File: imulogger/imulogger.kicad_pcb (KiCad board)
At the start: 2 copper layers, 64 x 25 mm, 31 parts, among them J1 DEBUG, J2 BATCONN, J4 Micro_SD_Card, J5 PWRCONN, Q1 TP0610T, U1 ESP32-WROOM-32, U2 USFS, U3 MCP1826S, U4 MCP73831-2-OT

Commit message: pcb: remove excessive vias close to the IMU
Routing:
- net GND: vias 67 -> 27
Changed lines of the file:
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@@
     (thickness 1.6)
     (drawings 12)
-    (tracks 488)
+    (tracks 448)
     (zones 0)
     (modules 31)
@@
   (segment (start 151.274999 67.774999) (end 145.651999 67.774999) (width 0.25) (layer B.Cu) (net 1))
   (segment (start 154 70.5) (end 151.274999 67.774999) (width 0.25) (layer B.Cu) (net 1) (status 10))
+  (segment (start 165.80237 71.54) (end 166.88 71.54) (width 0.4) (layer B.Cu) (net 1))
+  (segment (start 165.225001 75.675001) (end 165.225001 72.117369) (width 0.4) (layer B.Cu) (net 1))
+  (segment (start 148.325 81.3) (end 148.325 82.3) (width 0.4) (layer B.Cu) (net 1))
+  (segment (start 165.225001 72.117369) (end 165.80237 71.54) (width 0.4) (layer B.Cu) (net 1))
+  (segment (start 166.4 82.3) (end 166.4 76.85) (width 0.4) (layer B.Cu) (net 1))
+  (segment (start 166.4 76.85) (end 165.225001 75.675001) (width 0.4) (layer B.Cu) (net 1))
+  (segment (start 148.325 82.3) (end 148.925 82.9) (width 0.4) (layer B.Cu) (net 1))
+  (segment (start 148.925 82.9) (end 165.8 82.9) (width 0.4) (layer B.Cu) (net 1))
+  (segment (start 165.8 82.9) (end 166.4 82.3) (width 0.4) (layer B.Cu) (net 1))
   (via (at 156.65 70.175) (size 0.8) (drill 0.4) (layers F.Cu B.Cu) (net 2))
   (via (at 156.65 79.975) (size 0.8) (drill 0.4) (layers F.Cu B.Cu) (net 2))
@@
   (via (at 164.5 71.5) (size 0.8) (drill 0.4) (layers F.Cu B.Cu) (net 2))
   (via (at 164.5 76.5) (size 0.8) (drill 0.4) (layers F.Cu B.Cu) (net 2))
-  (via (at 170.5 76.5) (size 0.8) (drill 0.4) (layers F.Cu B.Cu) (net 2))
-  (segment (start 165.80237 71.54) (end 166.88 71.54) (width 0.4) (layer B.Cu) (net 1))
-  (segment (start 165.225001 75.675001) (end 165.225001 72.117369) (width 0.4) (layer B.Cu) (net 1))
-  (segment (start 148.325 81.3) (end 148.325 82.3) (width 0.4) (layer B.Cu) (net 1))
-  (segment (start 165.225001 72.117369) (end 165.80237 71.54) (width 0.4) (layer B.Cu) (net 1))
-  (segment (start 166.4 82.3) (end 166.4 76.85) (width 0.4) (layer B.Cu) (net 1))
-  (segment (start 166.4 76.85) (end 165.225001 75.675001) (width 0.4) (layer B.Cu) (net 1))
-  (segment (start 148.325 82.3) (end 148.925 82.9) (width 0.4) (layer B.Cu) (net 1))
-  (segment (start 148.925 82.9) (end 165.8 82.9) (width 0.4) (layer B.Cu) (net 1))
-  (segment (start 165.8 82.9) (end 166.4 82.3) (width 0.4) (layer B.Cu) (net 1))
-  (via (at 178.5 76.5) (size 0.8) (drill 0.4) (layers F.Cu B.Cu) (net 2))
-  (via (at 168.5 80.5) (size 0.8) (drill 0.4) (layers F.Cu B.Cu) (net 2))
-  (via (at 170.5 78.5) (size 0.8) (drill 0.4) (layers F.Cu B.Cu) (net 2))
-  (via (at 170.5 80.5) (size 0.8) (drill 0.4) (layers F.Cu B.Cu) (net 2))
-  (via (at 172.5 78.5) (size 0.8) (drill 0.4) (layers F.Cu B.Cu) (net 2))
-  (via (at 172.5 80.5) (size 0.8) (drill 0.4) (layers F.Cu B.Cu) (net 2))
-  (via (at 174.5 78.5) (size 0.8) (drill 0.4) (layers F.Cu B.Cu) (net 2))
-  (via (at 174.5 80.5) (size 0.8) (drill 0.4) (layers F.Cu B.Cu) (net 2))
-  (via (at 176.5 78.5) (size 0.8) (drill 0.4) (layers F.Cu B.Cu) (net 2))
-  (via (at 176.5 80.5) (size 0.8) (drill 0.4) (layers F.Cu B.Cu) (net 2))
-  (via (at 178.5 78.5) (size 0.8) (drill 0.4) (layers F.Cu B.Cu) (net 2))
   (via (at 128.5 62.5) (size 0.8) (drill 0.4) (layers F.Cu B.Cu) (net 2))
   (via (at 141.75 72.55) (size 0.8) (drill 0.4) (layers F.Cu B.Cu) (net 2))
@@
   (segment (start 168.4 74.588) (end 167.892 74.08) (width 0.25) (layer B.Cu) (net 2))
   (segment (start 168.4 77.35) (end 168.4 74.588) (width 0.25) (layer B.Cu) (net 2))
-  (via (at 178.5 80.5) (size 0.8) (drill 0.4) (layers F.Cu B.Cu) (net 2))
-  (via (at 181 76.5) (size 0.8) (drill 0.4) (layers F.Cu B.Cu) (net 2))
-  (via (at 181 78.5) (size 0.8) (drill 0.4) (layers F.Cu B.Cu) (net 2))
-  (via (at 181 80.5) (size 0.8) (drill 0.4) (layers F.Cu B.Cu) (net 2))
-  (via (at 181 82.5) (size 0.8) (drill 0.4) (layers F.Cu B.Cu) (net 2))
-  (via (at 178.5 82.5) (size 0.8) (drill 0.4) (layers F.Cu B.Cu) (net 2))
-  (via (at 176.5 82.5) (size 0.8) (drill 0.4) (layers F.Cu B.Cu) (net 2))
-  (via (at 174.5 82.5) (size 0.8) (drill 0.4) (layers F.Cu B.Cu) (net 2))
-  (via (at 172.5 82.5) (size 0.8) (drill 0.4) (layers F.Cu B.Cu) (net 2))
-  (via (at 170.5 82.5) (size 0.8) (drill 0.4) (layers F.Cu B.Cu) (net 2))
-  (via (at 168.5 82.5) (size 0.8) (drill 0.4) (layers F.Cu B.Cu) (net 2))
-  (via (at 182 60.5) (size 0.8) (drill 0.4) (layers F.Cu B.Cu) (net 2))
-  (via (at 182 62) (size 0.8) (drill 0.4) (layers F.Cu B.Cu) (net 2))
-  (via (at 180 62) (size 0.8) (drill 0.4) (layers F.Cu B.Cu) (net 2))
-  (via (at 178 62) (size 0.8) (drill 0.4) (layers F.Cu B.Cu) (net 2))
-  (via (at 176 62) (size 0.8) (drill 0.4) (layers F.Cu B.Cu) (net 2))
-  (via (at 174 62) (size 0.8) (drill 0.4) (layers F.Cu B.Cu) (net 2))
-  (via (at 172 62) (size 0.8) (drill 0.4) (layers F.Cu B.Cu) (net 2))
-  (via (at 170 62) (size 0.8) (drill 0.4) (layers F.Cu B.Cu) (net 2))
-  (via (at 180 60.5) (size 0.8) (drill 0.4) (layers F.Cu B.Cu) (net 2))
-  (via (at 178 60.5) (size 0.8) (drill 0.4) (layers F.Cu B.Cu) (net 2))
-  (via (at 176 60.5) (size 0.8) (drill 0.4) (layers F.Cu B.Cu) (net 2))
-  (via (at 174 60.5) (size 0.8) (drill 0.4) (layers F.Cu B.Cu) (net 2))
-  (via (at 172 60.5) (size 0.8) (drill 0.4) (layers F.Cu B.Cu) (net 2))
-  (via (at 170 60.5) (size 0.8) (drill 0.4) (layers F.Cu B.Cu) (net 2))
-  (via (at 176.5 76.5) (size 0.8) (drill 0.4) (layers F.Cu B.Cu) (net 2))
-  (via (at 174.5 76.5) (size 0.8) (drill 0.4) (layers F.Cu B.Cu) (net 2))
-  (via (at 172.5 76.5) (size 0.8) (drill 0.4) (layers F.Cu B.Cu) (net 2))
   (segment (start 133.499999 62.075001) (end 132.174999 62.075001) (width 0.25) (layer F.Cu) (net 2))
   (segment (start 134.675 60.9) (end 133.499999 62.075001) (width 0.25) (layer F.Cu) (net 2))

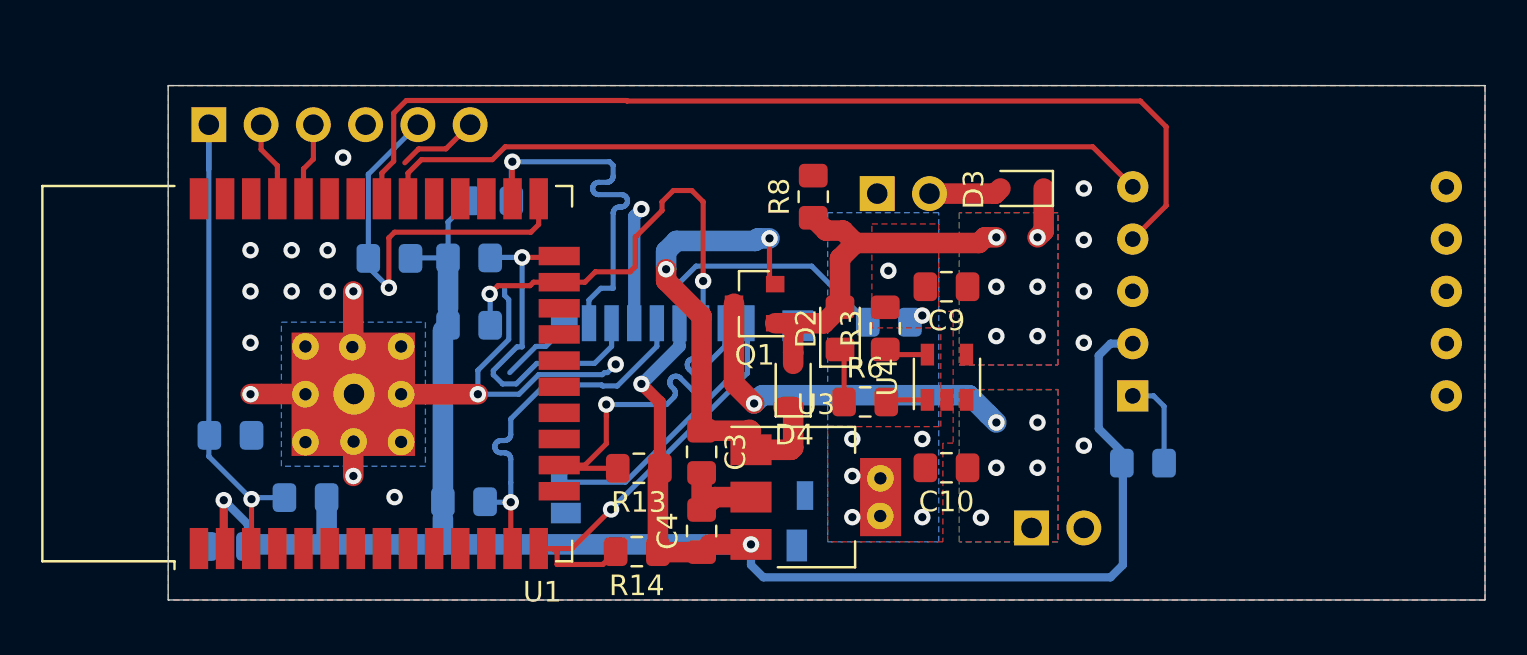
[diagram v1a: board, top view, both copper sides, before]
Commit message: imulogger: pcb: reroute i2c and optimize ground fillings
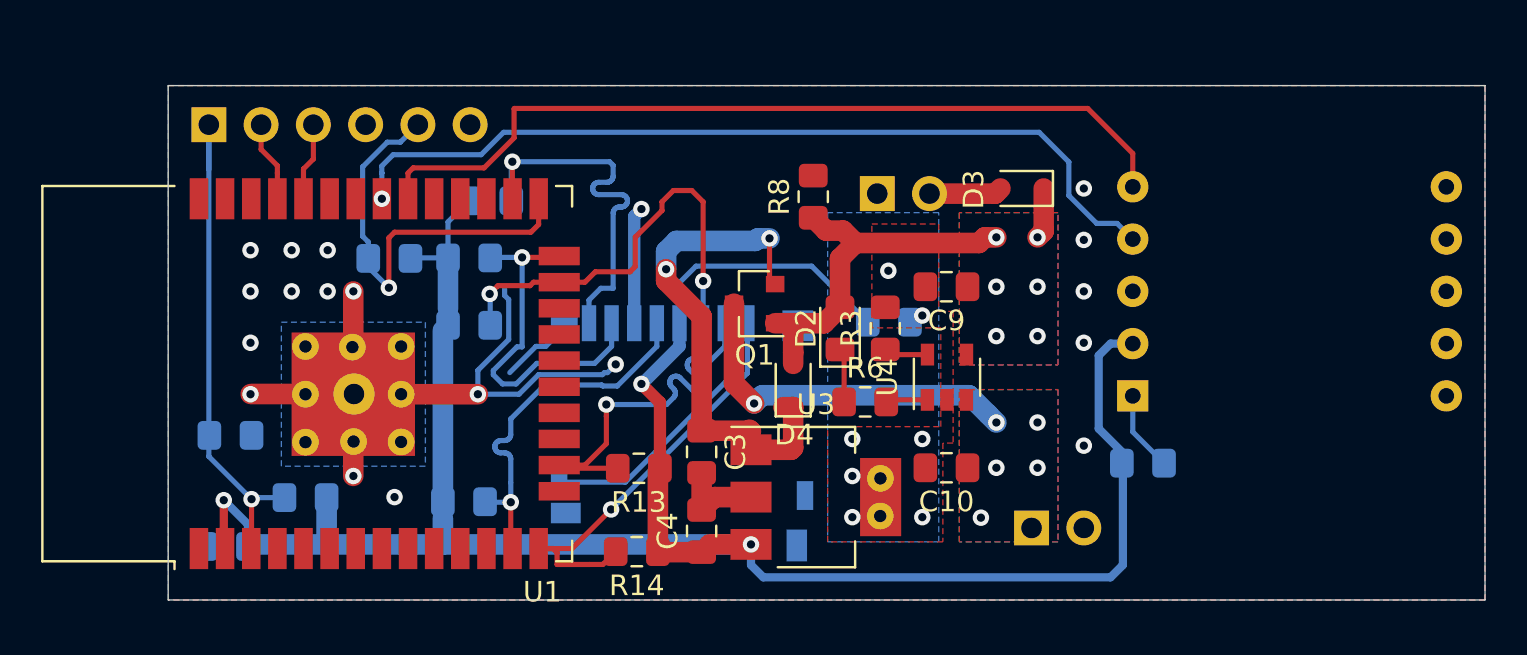
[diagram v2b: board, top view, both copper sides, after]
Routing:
- net IMU_SCL: track 48.9 -> 41.9 mm, vias 0 -> 1
- net GND: track 70.1 -> 65.6 mm, vias 27 -> 26
- net IMU_SDA: track 37.8 -> 41.1 mm
- net IO0: track 20.7 -> 21.3 mm
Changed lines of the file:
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@@
-(kicad_pcb (version 20171130) (host pcbnew 5.1.0)
+(kicad_pcb (version 20171130) (host pcbnew 5.1.2)
   (general
     (thickness 1.6)
     (drawings 12)
-    (tracks 448)
+    (tracks 453)
     (zones 0)
     (modules 31)
@@
     (last_trace_width 0.25)
     (trace_clearance 0.2)
-    (zone_clearance 0.5)
+    (zone_clearance 0.25)
     (zone_45_only no)
     (trace_min 0.2)
@@
   (via (at 164.5 71.5) (size 0.8) (drill 0.4) (layers F.Cu B.Cu) (net 2))
   (via (at 164.5 76.5) (size 0.8) (drill 0.4) (layers F.Cu B.Cu) (net 2))
-  (via (at 128.5 62.5) (size 0.8) (drill 0.4) (layers F.Cu B.Cu) (net 2))
   (via (at 141.75 72.55) (size 0.8) (drill 0.4) (layers F.Cu B.Cu) (net 2))
   (via (at 135.05 74) (size 0.8) (drill 0.4) (layers F.Cu B.Cu) (net 2))
@@
   (segment (start 142.21359 78.275) (end 147.65 72.83859) (width 0.25) (layer B.Cu) (net 2))
   (segment (start 147.65 72.83859) (end 147.65 72.4) (width 0.25) (layer B.Cu) (net 2))
-  (segment (start 167.892 74.08) (end 166.88 74.08) (width 0.25) (layer B.Cu) (net 2))
-  (segment (start 168.4 74.588) (end 167.892 74.08) (width 0.25) (layer B.Cu) (net 2))
-  (segment (start 168.4 77.35) (end 168.4 74.588) (width 0.25) (layer B.Cu) (net 2))
-  (segment (start 133.499999 62.075001) (end 132.174999 62.075001) (width 0.25) (layer F.Cu) (net 2))
-  (segment (start 134.675 60.9) (end 133.499999 62.075001) (width 0.25) (layer F.Cu) (net 2))
-  (segment (start 132.174999 62.075001) (end 131.5 62.75) (width 0.25) (layer F.Cu) (net 2))
   (via (at 124 67) (size 0.8) (drill 0.4) (layers F.Cu B.Cu) (net 2))
   (via (at 126 67) (size 0.8) (drill 0.4) (layers F.Cu B.Cu) (net 2))
@@
   (segment (start 128.995 69.005) (end 129 69) (width 0.25) (layer F.Cu) (net 2))
   (segment (start 128.995 74) (end 128.995 69.005) (width 1) (layer F.Cu) (net 2))
+  (segment (start 166.88 75.83) (end 166.88 74.08) (width 0.25) (layer B.Cu) (net 2))
+  (segment (start 168.4 77.35) (end 166.88 75.83) (width 0.25) (layer B.Cu) (net 2))
   (via (at 124.05 79.1) (size 0.8) (drill 0.4) (layers F.Cu B.Cu) (net 3))
   (segment (start 125.65 79.025) (end 124.125 79.025) (width 0.25) (layer B.Cu) (net 3) (status 10))
@@
   (segment (start 129.725 67.4) (end 129.725 67.825) (width 0.25) (layer B.Cu) (net 6) (status 30))
   (segment (start 129.725 67.825) (end 130.725 68.825) (width 0.25) (layer B.Cu) (net 6) (status 10))
+  (segment (start 131.285001 61.749999) (end 130.650001 61.749999) (width 0.25) (layer B.Cu) (net 6))
+  (segment (start 132.135 60.9) (end 131.285001 61.749999) (width 0.25) (layer B.Cu) (net 6))
+  (segment (start 129.725 66.6) (end 129.725 67.4) (width 0.25) (layer B.Cu) (net 6))
+  (segment (start 129.45 66.325) (end 129.725 66.6) (width 0.25) (layer B.Cu) (net 6))
+  (segment (start 129.45 62.95) (end 129.45 66.325) (width 0.25) (layer B.Cu) (net 6))
+  (segment (start 130.650001 61.749999) (end 129.45 62.95) (width 0.25) (layer B.Cu) (net 6))
+  (segment (start 130.725 66.4) (end 131 66.125) (width 0.25) (layer F.Cu) (net 6))
   (segment (start 130.725 68.825) (end 130.725 66.4) (width 0.25) (layer F.Cu) (net 6))
-  (segment (start 130.725 66.4) (end 131 66.125) (width 0.25) (layer F.Cu) (net 6))
+  (segment (start 131 66.125) (end 137.63 66.125) (width 0.25) (layer F.Cu) (net 6))
+  (segment (start 137.63 66.125) (end 138.005 65.75) (width 0.25) (layer F.Cu) (net 6))
   (segment (start 138.005 65.75) (end 138.005 64.5) (width 0.25) (layer F.Cu) (net 6) (status 20))
-  (segment (start 137.63 66.125) (end 138.005 65.75) (width 0.25) (layer F.Cu) (net 6))
-  (segment (start 131 66.125) (end 137.63 66.125) (width 0.25) (layer F.Cu) (net 6))
-  (segment (start 129.725 63.31) (end 129.725 67.4) (width 0.25) (layer B.Cu) (net 6) (status 20))
-  (segment (start 132.135 60.9) (end 129.725 63.31) (width 0.25) (layer B.Cu) (net 6) (status 10))
   (via (at 136.725 62.7) (size 0.8) (drill 0.4) (layers F.Cu B.Cu) (net 7))
   (segment (start 136.725 64.49) (end 136.735 64.5) (width 0.25) (layer F.Cu) (net 7) (status 30))
@@
   (segment (start 138.9 81.695) (end 138.705 81.5) (width 0.25) (layer F.Cu) (net 12))
   (segment (start 138.9 82.275) (end 138.9 81.695) (width 0.25) (layer F.Cu) (net 12))
-  (segment (start 131.655 64.5) (end 131.655 63.25) (width 0.25) (layer F.Cu) (net 13) (status 10))
-  (segment (start 131.655 63.25) (end 132.305 62.6) (width 0.25) (layer F.Cu) (net 13))
-  (segment (start 135.751998 62.6) (end 136.376999 61.974999) (width 0.25) (layer F.Cu) (net 13))
-  (segment (start 132.305 62.6) (end 135.751998 62.6) (width 0.25) (layer F.Cu) (net 13))
-  (segment (start 164.934999 61.974999) (end 166.88 63.92) (width 0.25) (layer F.Cu) (net 13))
-  (segment (start 136.376999 61.974999) (end 164.934999 61.974999) (width 0.25) (layer F.Cu) (net 13))
-  (segment (start 130.959999 60.335999) (end 131.570999 59.724999) (width 0.25) (layer F.Cu) (net 14))
-  (segment (start 130.959999 62.675001) (end 130.959999 60.335999) (width 0.25) (layer F.Cu) (net 14))
-  (segment (start 130.385 64.5) (end 130.385 63.25) (width 0.25) (layer F.Cu) (net 14) (status 10))
-  (segment (start 130.385 63.25) (end 130.959999 62.675001) (width 0.25) (layer F.Cu) (net 14))
-  (segment (start 142.275001 59.724999) (end 142.300002 59.75) (width 0.25) (layer F.Cu) (net 14))
-  (segment (start 131.570999 59.724999) (end 142.275001 59.724999) (width 0.25) (layer F.Cu) (net 14))
-  (segment (start 142.300002 59.75) (end 167.25 59.75) (width 0.25) (layer F.Cu) (net 14))
-  (segment (start 167.25 59.75) (end 168.5 61) (width 0.25) (layer F.Cu) (net 14))
-  (segment (start 168.5 64.84) (end 166.88 66.46) (width 0.25) (layer F.Cu) (net 14))
-  (segment (start 168.5 61) (end 168.5 64.84) (width 0.25) (layer F.Cu) (net 14))
+  (segment (start 136.81 60.13) (end 136.83 60.11) (width 0.25) (layer F.Cu) (net 13))
+  (segment (start 135.351998 63) (end 136.81 61.541998) (width 0.25) (layer F.Cu) (net 13))
+  (segment (start 131.905 63) (end 135.351998 63) (width 0.25) (layer F.Cu) (net 13))
+  (segment (start 131.655 64.5) (end 131.655 63.25) (width 0.25) (layer F.Cu) (net 13))
+  (segment (start 136.81 61.541998) (end 136.81 60.13) (width 0.25) (layer F.Cu) (net 13))
+  (segment (start 131.655 63.25) (end 131.905 63) (width 0.25) (layer F.Cu) (net 13))
+  (segment (start 136.83 60.11) (end 164.69 60.11) (width 0.25) (layer F.Cu) (net 13))
+  (segment (start 164.69 60.11) (end 166.88 62.3) (width 0.25) (layer F.Cu) (net 13))
+  (segment (start 166.88 62.3) (end 166.88 63.92) (width 0.25) (layer F.Cu) (net 13))
+  (via (at 130.385 64.5) (size 0.8) (drill 0.4) (layers F.Cu B.Cu) (net 14))
+  (segment (start 165.124999 65.698001) (end 166.118001 65.698001) (width 0.25) (layer B.Cu) (net 14))
+  (segment (start 163.774999 64.348001) (end 165.124999 65.698001) (width 0.25) (layer B.Cu) (net 14))
+  (segment (start 163.774999 62.714999) (end 163.774999 64.348001) (width 0.25) (layer B.Cu) (net 14))
+  (segment (start 162.33 61.27) (end 163.774999 62.714999) (width 0.25) (layer B.Cu) (net 14))
+  (segment (start 136.3 61.27) (end 162.33 61.27) (width 0.25) (layer B.Cu) (net 14))
+  (segment (start 166.118001 65.698001) (end 166.88 66.46) (width 0.25) (layer B.Cu) (net 14))
+  (segment (start 130.385 63.25) (end 130.38 63.245) (width 0.25) (layer B.Cu) (net 14))
+  (segment (start 130.93 62.36) (end 135.21 62.36) (width 0.25) (layer B.Cu) (net 14))
+  (segment (start 135.21 62.36) (end 136.3 61.27) (width 0.25) (layer B.Cu) (net 14))
+  (segment (start 130.385 64.5) (end 130.385 63.25) (width 0.25) (layer B.Cu) (net 14))
+  (segment (start 130.38 63.245) (end 130.38 62.91) (width 0.25) (layer B.Cu) (net 14))
+  (segment (start 130.38 62.91) (end 130.93 62.36) (width 0.25) (layer B.Cu) (net 14))
   (segment (start 148.575 76.7) (end 148.325 76.7) (width 0.25) (layer F.Cu) (net 15) (status 30))
   (segment (start 148.325 76.7) (end 148.325 75.8) (width 0.25) (layer F.Cu) (net 15) (status 10))
@@
   )
   (zone (net 2) (net_name GND) (layer F.Cu) (hatch edge 0.508)
-    (connect_pads (clearance 0.3))
+    (connect_pads (clearance 0.25))
     (min_thickness 0.254)
     (fill yes (arc_segments 32) (thermal_gap 0.508) (thermal_bridge_width 0.508))
@@
   )
   (zone (net 2) (net_name GND) (layer B.Cu) (hatch edge 0.508)
-    (connect_pads (clearance 0.3))
+    (connect_pads (clearance 0.25))
     (min_thickness 0.254)
     (fill yes (arc_segments 32) (thermal_gap 0.508) (thermal_bridge_width 0.508))

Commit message: imulogger: add battery protection circuit
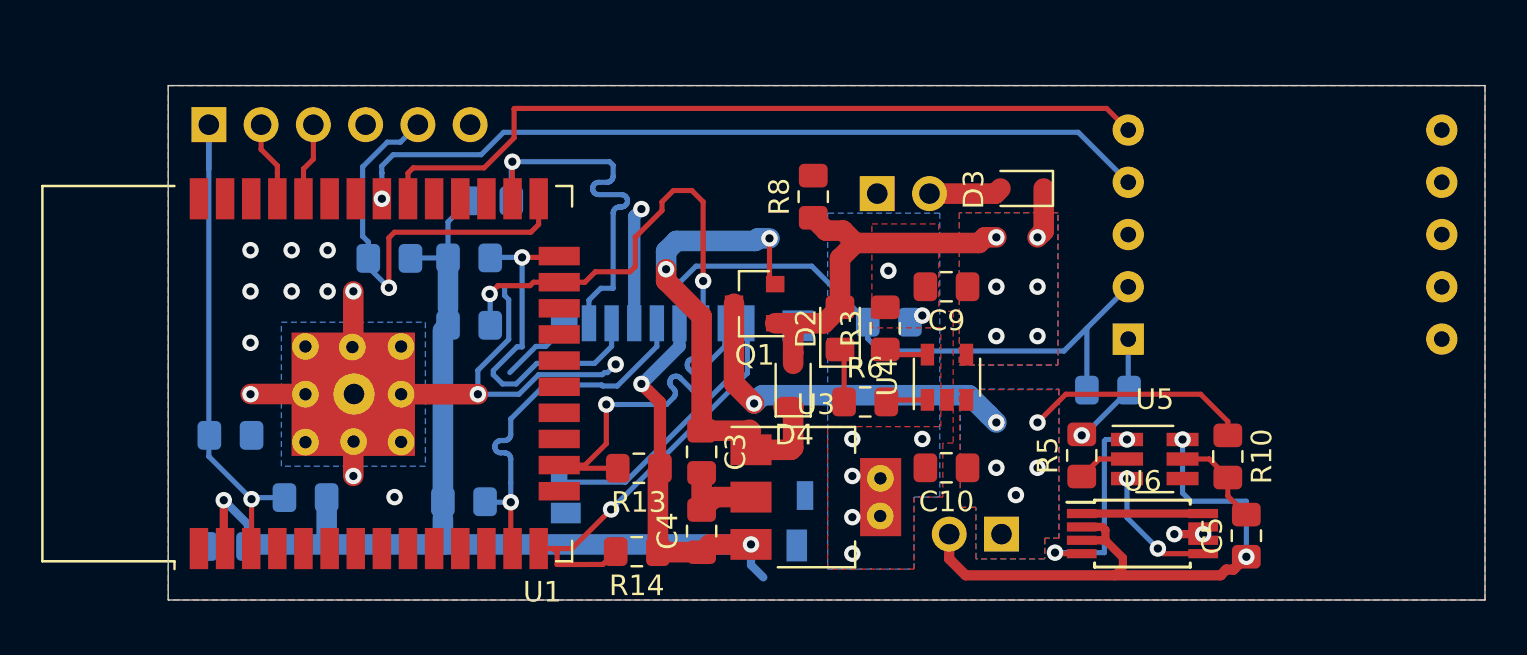
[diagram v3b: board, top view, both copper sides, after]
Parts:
- added C5: 100n, Capacitor_SMD:C_0805_2012Metric_Pad1.15x1.40mm_HandSolder, F.Cu at (172.4, 80.9)
- added R10: 100, Resistor_SMD:R_0805_2012Metric_Pad1.15x1.40mm_HandSolder, F.Cu at (171.5, 77.0)
- added R5: 2K, Resistor_SMD:R_0805_2012Metric_Pad1.15x1.40mm_HandSolder, F.Cu at (164.4, 77.0)
- added U5: dw01, Package_TO_SOT_SMD:SOT-23-6_Handsoldering, F.Cu at (167.9, 77.2)
- added U6: FS8205A, Package_SO:TSSOP-8_4.4x3mm_P0.65mm, F.Cu at (167.3, 80.8)
- moved C8 3.94 mm to (165.7, 73.8)
- moved U2 2.77 mm to (174.3, 66.2)
- moved J2 1.49 mm to (160.5, 80.8), turned to 90 degrees
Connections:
- J2 pad 2: GND -> Net-(C5-Pad1)
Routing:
- net Net-(C5-Pad1): track 0.00 -> 30.6 mm, vias 0 -> 2
- net +3V3: track 112.9 -> 100.6 mm
- net V_BAT: track 17.7 -> 28.8 mm
- net Net-(U5-Pad1): track 0.00 -> 10.3 mm, vias 0 -> 2
- net Net-(U5-Pad3): track 0.00 -> 6.32 mm, vias 0 -> 2
- net Net-(U6-Pad1): track 0.00 -> 5.90 mm
- net Net-(C5-Pad2): track 0.00 -> 4.75 mm
- net GND: track 65.6 -> 69.5 mm, vias 26 -> 24
- net Net-(R5-Pad1): track 0.00 -> 2.55 mm
- net IMU_SCL: track 41.9 -> 39.6 mm
- net IMU_SDA: track 41.1 -> 38.8 mm
